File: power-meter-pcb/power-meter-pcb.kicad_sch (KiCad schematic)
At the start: 12 parts, among them J1 USB4105-GF-A, J2 Debug, SW1 EN, SW2 BOOT, U1 TPD3E001DRLR, U2 ESP32-S3-WROOM-1

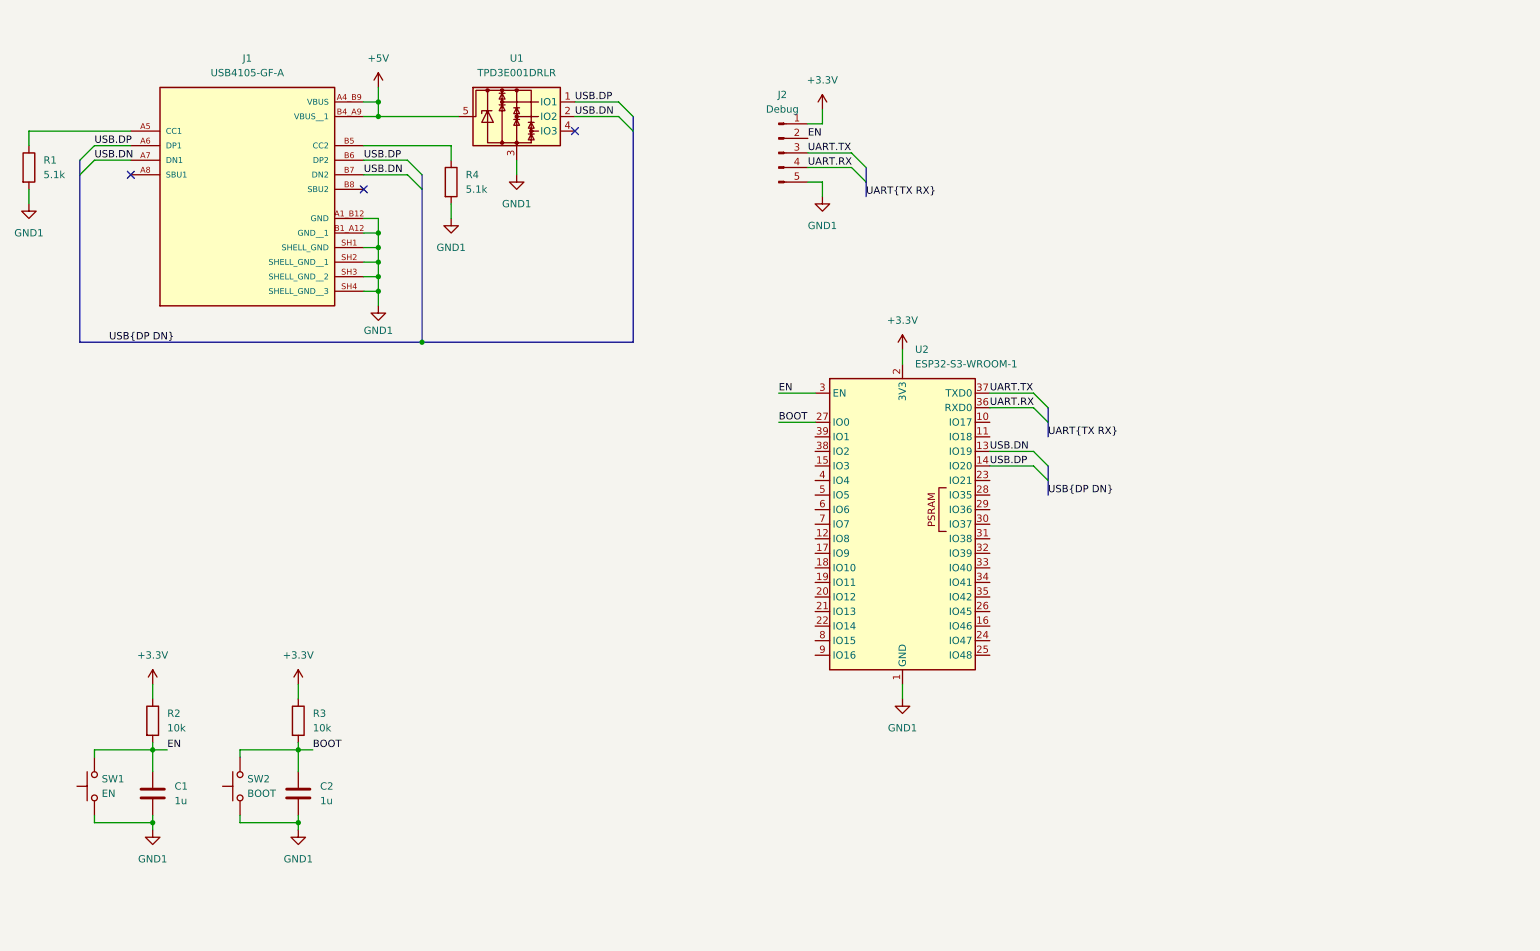
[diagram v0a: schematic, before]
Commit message: Added amplifier, IMU, inter board connections
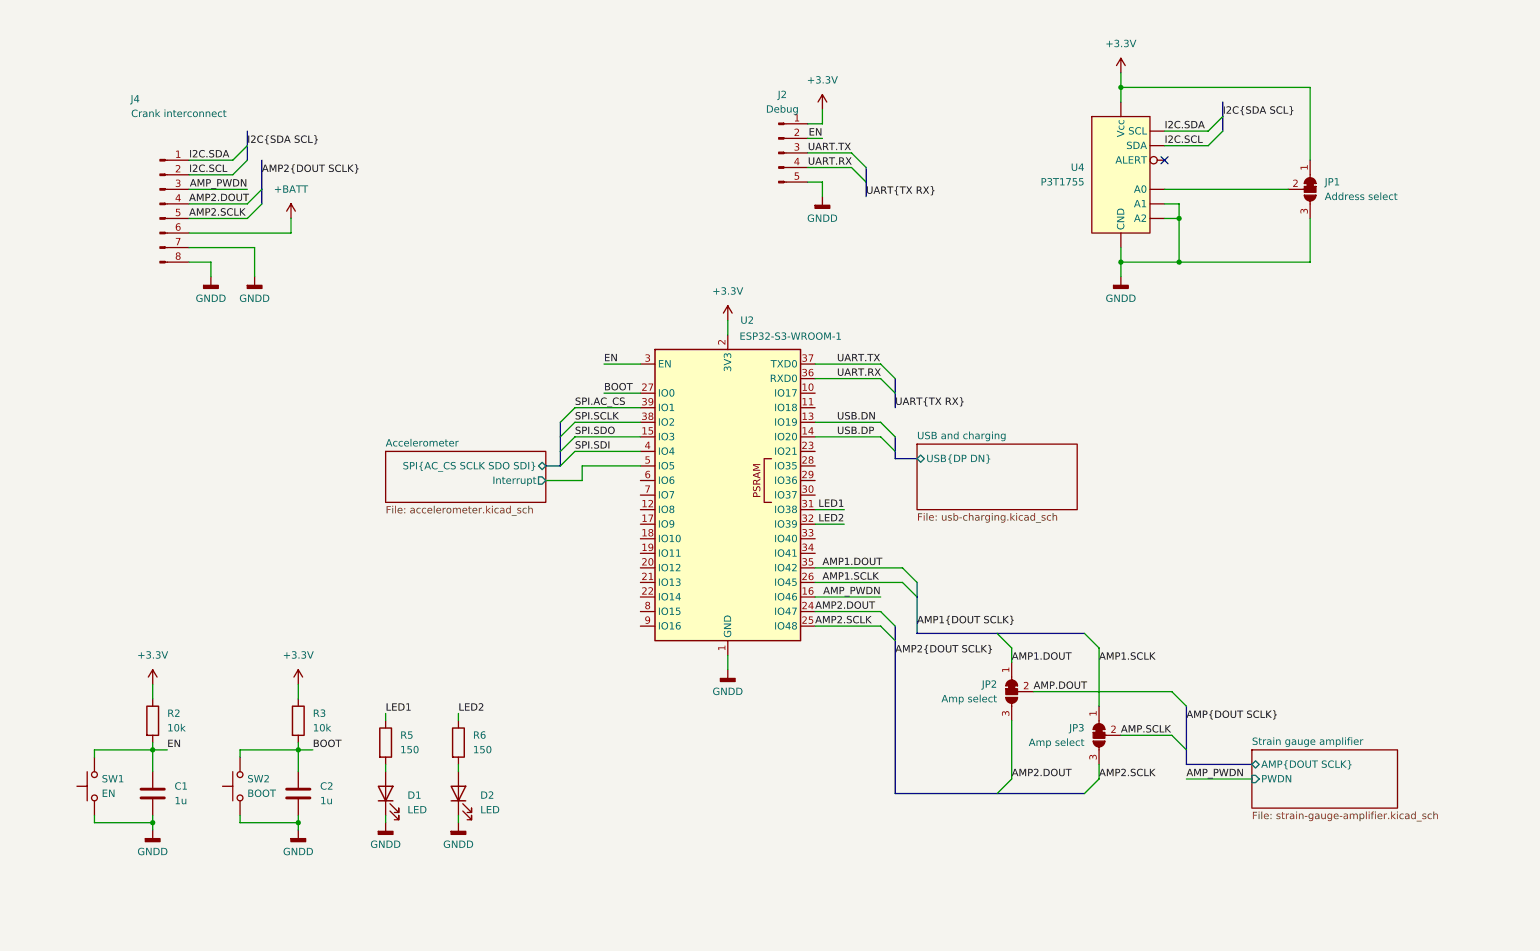
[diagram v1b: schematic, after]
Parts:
- removed J1: USB4105-GF-A, USB4105-GF-A:GCT_USB4105-GF-A, symbol USB4105:USB4105-GF-A
- removed R1, R4: 5.1k, symbol Device:R
- removed U1: TPD3E001DRLR, Package_TO_SOT_SMD:SOT-553, symbol Power_Protection:TPD3E001DRLR
- added D1, D2: LED, symbol Device:LED
- added J4: Crank interconnect, symbol Connector:Conn_01x08_Pin
- added JP1: Address select, symbol Jumper:SolderJumper_3_Bridged12
- added JP2, JP3: Amp select, symbol Jumper:SolderJumper_3_Bridged12
- added R5, R6: 150, symbol Device:R
- added U4: P3T1755, Package_SO:TSSOP-8_3x3mm_P0.65mm, symbol Custom:P3T1755_Temperature_sensor
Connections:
- net +3.3V: now also JP1.1 (A), U4. (Vcc)
- net SPI.SDO: now reaches U2.15 (IO3)
- net AMP_PWDN: now reaches U2.16 (IO46)
- net AMP_PWDN: now also J4.3 (Pin_3)
- net AMP2.DOUT: now reaches U2.24 (IO47)
- net AMP2.DOUT: now also J4.4 (Pin_4), JP2.3 (B)
- net AMP2.SCLK: now reaches U2.25 (IO48)
- net AMP2.SCLK: now also J4.5 (Pin_5), JP3.3 (B)
- net AMP1.SCLK: now reaches U2.26 (IO45)
- net AMP1.SCLK: now also JP3.1 (A)
- net LED1: now reaches U2.31 (IO38)
- net LED1: now also R5.1
- net LED2: now reaches U2.32 (IO39)
- net LED2: now also R6.1
- net AMP1.DOUT: now reaches U2.35 (IO42)
- net AMP1.DOUT: now also JP2.1 (A)
- net SPI.SCLK: now reaches U2.38 (IO2)
- net SPI.AC_CS: now reaches U2.39 (IO1)
- net SPI.SDI: now reaches U2.4 (IO4)
- net Accelerometer/Interrupt: now reaches U2.5 (IO5)
- net GND1 renamed GNDD
- net GNDD: now also D1.1 (K), D2.1 (K), J4.7 (Pin_7), J4.8 (Pin_8), JP1.3 (B), U4. (Vcc)
- new net: JP1.2 (C), U4. (Vcc)
- new net: D2.2 (A), R6.2
- new net: D1.2 (A), R5.2
- new net +BATT: J4.6 (Pin_6)
- new net AMP.DOUT: JP2.2 (C)
- new net AMP.SCLK: JP3.2 (C)
- new net I2C.SCL: J4.2 (Pin_2), U4. (Vcc)
- new net I2C.SDA: J4.1 (Pin_1), U4. (Vcc)
- no-connect marks 3 -> 1
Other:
- added sheet Accelerometer (accelerometer.kicad_sch)
- added sheet Strain gauge amplifier (strain-gauge-amplifier.kicad_sch)
- added sheet USB and charging (usb-charging.kicad_sch)
- moved on the sheet: U2

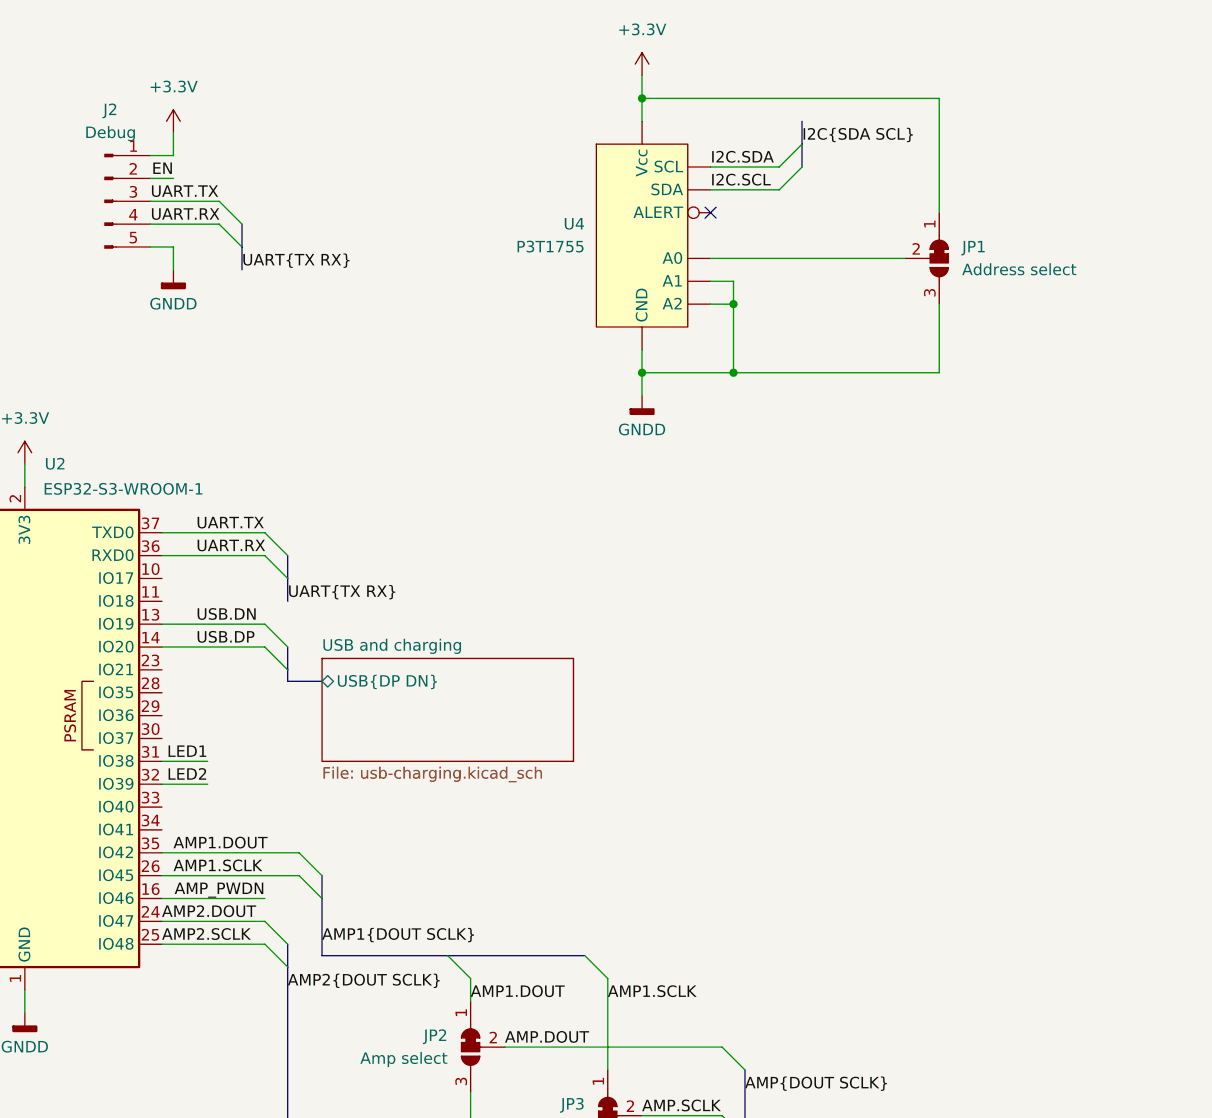
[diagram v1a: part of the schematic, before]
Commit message: Assigning footprints, extremely rough idea of size
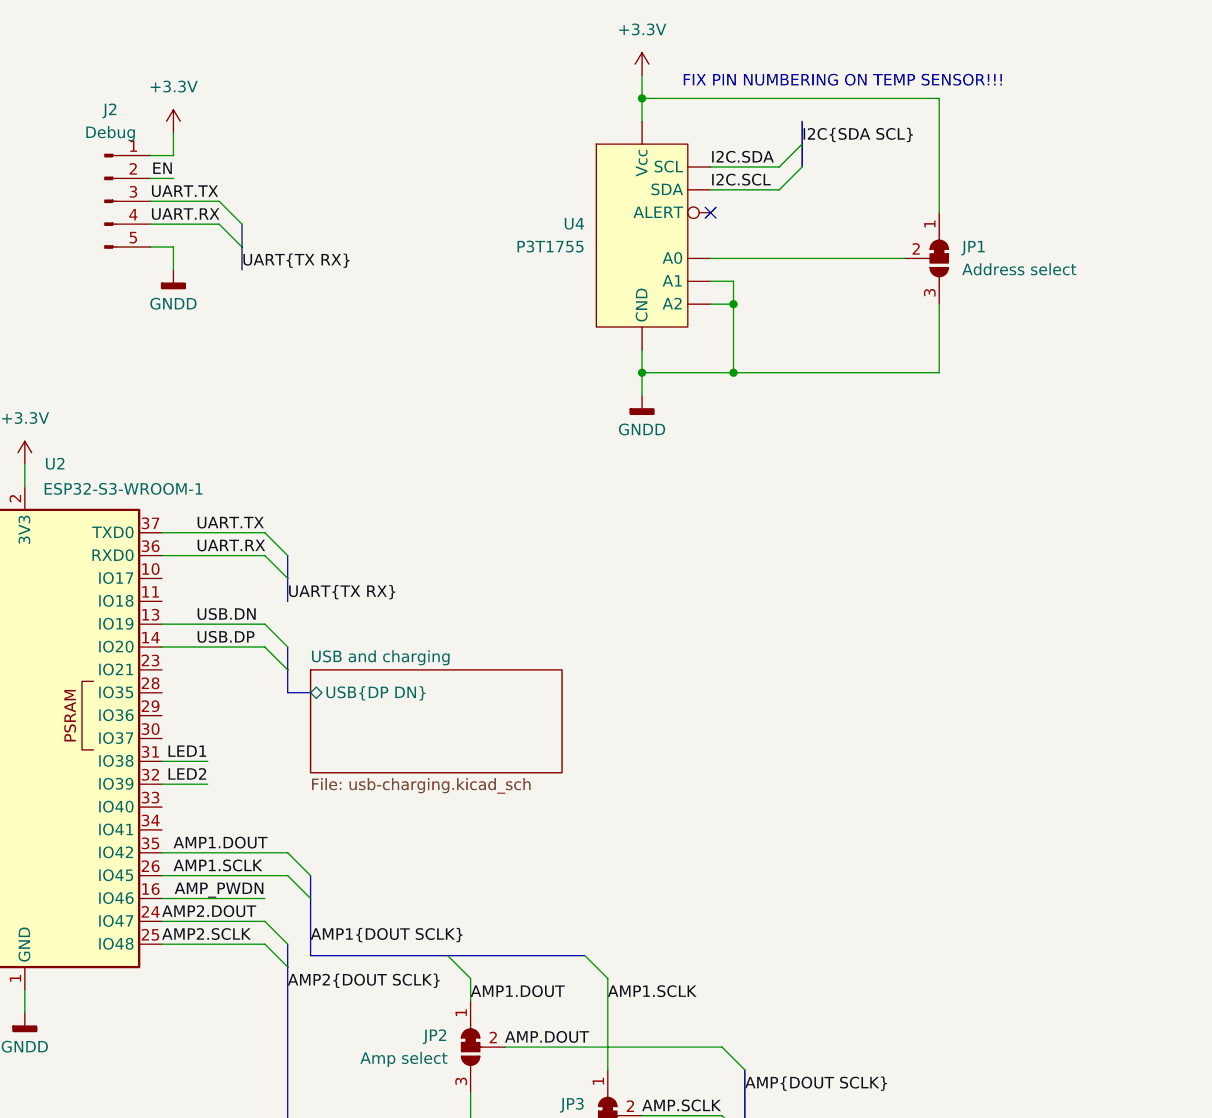
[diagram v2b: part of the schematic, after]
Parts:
- C1, C2: footprint (none) -> Capacitor_SMD:C_0603_1608Metric_Pad1.08x0.95mm_HandSolder
- D1, D2: footprint (none) -> LED_SMD:LED_0603_1608Metric_Pad1.05x0.95mm_HandSolder
- J2: footprint (none) -> Connector_PinHeader_2.54mm:PinHeader_1x05_P2.54mm_Vertical
- J4: footprint (none) -> Connector_PinHeader_2.54mm:PinHeader_1x08_P2.54mm_Vertical
- JP1, JP2, JP3: footprint (none) -> Jumper:SolderJumper-3_P1.3mm_Open_RoundedPad1.0x1.5mm
- R2, R3, R5, R6: footprint (none) -> Resistor_SMD:R_0603_1608Metric_Pad0.98x0.95mm_HandSolder
- SW1, SW2: footprint (none) -> Button_Switch_SMD:SW_Push_1P1T_NO_CK_KMR2
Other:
- note added: "FIX PIN NUMBERING ON TEMP SENSOR!!!"
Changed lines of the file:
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@@
 	)
 	(bus_entry
-		(at 176.53 121.92)
+		(at 175.26 121.92)
 		(size 2.54 2.54)
 		(stroke
@@
 	)
 	(bus_entry
-		(at 176.53 124.46)
+		(at 175.26 124.46)
 		(size 2.54 2.54)
 		(stroke
@@
 	(bus
 		(pts
-			(xy 179.07 102.87) (xy 175.26 102.87)
+			(xy 177.8 104.14) (xy 175.26 104.14)
 		)
 		(stroke
@@
 	(bus
 		(pts
-			(xy 179.07 127) (xy 179.07 133.35)
+			(xy 177.8 127) (xy 177.8 133.35)
 		)
 		(stroke
@@
 	(bus
 		(pts
-			(xy 175.26 101.6) (xy 175.26 102.87)
+			(xy 175.26 101.6) (xy 175.26 104.14)
 		)
 		(stroke
@@
 	(wire
 		(pts
-			(xy 161.29 121.92) (xy 176.53 121.92)
+			(xy 161.29 121.92) (xy 175.26 121.92)
 		)
 		(stroke
@@
 	(bus
 		(pts
-			(xy 179.07 133.35) (xy 193.04 133.35)
+			(xy 177.8 133.35) (xy 193.04 133.35)
 		)
 		(stroke
@@
 	(wire
 		(pts
-			(xy 161.29 124.46) (xy 176.53 124.46)
+			(xy 161.29 124.46) (xy 175.26 124.46)
 		)
 		(stroke
@@
 	(bus
 		(pts
-			(xy 179.07 124.46) (xy 179.07 127)
+			(xy 177.8 124.46) (xy 177.8 127)
 		)
 		(stroke
@@
 		)
 	)
+	(text "FIX PIN NUMBERING ON TEMP SENSOR!!!"
+		(exclude_from_sim no)
+		(at 236.982 36.322 0)
+		(effects
+			(font
+				(size 1.27 1.27)
+			)
+		)
+	)
 	(label "BOOT"
 		(at 73.66 153.67 0)
@@
 	)
 	(label "AMP1{DOUT SCLK}"
-		(at 179.07 132.08 0)
+		(at 177.8 132.08 0)
 		(fields_autoplaced yes)
 		(effects
@@
 			)
 		)
-		(property "Footprint" ""
+		(property "Footprint" "Button_Switch_SMD:SW_Push_1P1T_NO_CK_KMR2"
 			(at 30.48 160.02 0)
 			(effects
@@
 			)
 		)
-		(property "Footprint" ""
+		(property "Footprint" "Jumper:SolderJumper-3_P1.3mm_Open_RoundedPad1.0x1.5mm"
 			(at 195.58 143.51 0)
 			(effects
@@
 			)
 		)
-		(property "Footprint" ""
+		(property "Footprint" "Capacitor_SMD:C_0603_1608Metric_Pad1.08x0.95mm_HandSolder"
 			(at 44.7548 157.48 0)
 			(effects
@@
 			)
 		)
-		(property "Footprint" ""
+		(property "Footprint" "Connector_PinHeader_2.54mm:PinHeader_1x08_P2.54mm_Vertical"
 			(at 46.99 58.42 0)
 			(effects
@@
 			)
 		)
-		(property "Footprint" ""
+		(property "Footprint" "Resistor_SMD:R_0603_1608Metric_Pad0.98x0.95mm_HandSolder"
 			(at 43.942 148.59 90)
 			(effects
@@
 			)
 		)
-		(property "Footprint" ""
+		(property "Footprint" "Resistor_SMD:R_0603_1608Metric_Pad0.98x0.95mm_HandSolder"
 			(at 69.342 148.59 90)
 			(effects
@@
 			)
 		)
-		(property "Footprint" ""
+		(property "Footprint" "Resistor_SMD:R_0603_1608Metric_Pad0.98x0.95mm_HandSolder"
 			(at 97.282 152.4 90)
 			(effects
@@
 			)
 		)
-		(property "Footprint" ""
+		(property "Footprint" "Connector_PinHeader_2.54mm:PinHeader_1x05_P2.54mm_Vertical"
 			(at 154.94 49.53 0)
 			(effects
@@
 			)
 		)
-		(property "Footprint" ""
+		(property "Footprint" "Button_Switch_SMD:SW_Push_1P1T_NO_CK_KMR2"
 			(at 55.88 160.02 0)
 			(effects
@@
 			)
 		)
-		(property "Footprint" ""
+		(property "Footprint" "Jumper:SolderJumper-3_P1.3mm_Open_RoundedPad1.0x1.5mm"
 			(at 247.65 55.88 0)
 			(effects
@@
 			)
 		)
-		(property "Footprint" ""
+		(property "Footprint" "LED_SMD:LED_0603_1608Metric_Pad1.05x0.95mm_HandSolder"
 			(at 86.36 161.29 0)
 			(effects
@@
 			)
 		)
-		(property "Footprint" ""
+		(property "Footprint" "LED_SMD:LED_0603_1608Metric_Pad1.05x0.95mm_HandSolder"
 			(at 99.06 161.29 0)
 			(effects
@@
 			)
 		)
-		(property "Footprint" ""
+		(property "Footprint" "Resistor_SMD:R_0603_1608Metric_Pad0.98x0.95mm_HandSolder"
 			(at 84.582 152.4 90)
 			(effects
@@
 			)
 		)
-		(property "Footprint" ""
+		(property "Footprint" "Jumper:SolderJumper-3_P1.3mm_Open_RoundedPad1.0x1.5mm"
 			(at 210.82 151.13 0)
 			(effects
@@
 			)
 		)
-		(property "Footprint" ""
+		(property "Footprint" "Capacitor_SMD:C_0603_1608Metric_Pad1.08x0.95mm_HandSolder"
 			(at 70.1548 157.48 0)
 			(effects
@@
 	)
 	(sheet
-		(at 179.07 100.33)
+		(at 177.8 101.6)
 		(size 27.94 11.43)
 		(fields_autoplaced yes)
@@
 		)
 		(property "Sheetname" "USB and charging"
-			(at 179.07 99.6184 0)
+			(at 177.8 100.8884 0)
 			(effects
 				(font
@@
 		)
 		(property "Sheetfile" "usb-charging.kicad_sch"
-			(at 179.07 112.3446 0)
+			(at 177.8 113.6146 0)
 			(effects
 				(font
@@
 		)
 		(pin "USB{DP DN}" bidirectional
-			(at 179.07 102.87 180)
+			(at 177.8 104.14 180)
 			(effects
 				(font

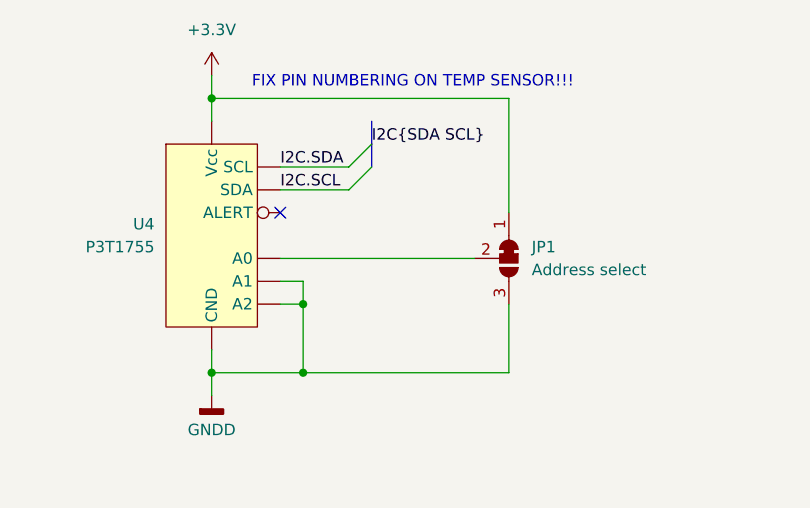
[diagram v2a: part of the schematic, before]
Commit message: Added power supply to PCB
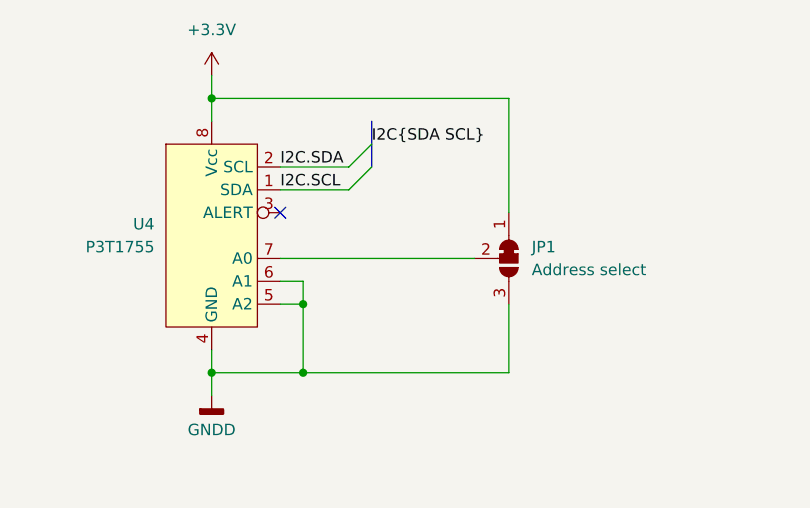
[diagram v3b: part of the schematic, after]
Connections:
- net +3.3V: now also U4.8 (Vcc); no longer U4. (Vcc)
- net GNDD: now also U4.4 (GND), U4.5 (A2), U4.6 (A1); no longer U4. (Vcc)
- net I2C.SCL: now also U4.1 (SDA); no longer U4. (Vcc)
- net I2C.SDA: now also U4.2 (SCL); no longer U4. (Vcc)
- net at JP1.2 (C): now also U4.7 (A0); no longer U4. (Vcc)
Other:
- note removed: "FIX PIN NUMBERING ON TEMP SENSOR!!!"
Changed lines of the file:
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@@
-		)
-	)
-	(text "FIX PIN NUMBERING ON TEMP SENSOR!!!"
-		(exclude_from_sim no)
-		(at 236.982 36.322 0)
-		(effects
-			(font
-				(size 1.27 1.27)
-			)
 		)
 	)
@@
 			)
 		)
-		(pin ""
-		)
-		(pin ""
-		)
-		(pin ""
-		)
-		(pin ""
-		)
-		(pin ""
-		)
-		(pin ""
-		)
-		(pin ""
-		)
-		(pin ""
+		(pin "8"
+		)
+		(pin "2"
+		)
+		(pin "6"
+		)
+		(pin "4"
+		)
+		(pin "3"
+		)
+		(pin "1"
+		)
+		(pin "5"
+		)
+		(pin "7"
 		)
 		(instances

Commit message: Started PCB layout
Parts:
- renumbered J4 to J1, JP2 to JP1, JP3 to JP2, JP1 to JP3, R2 to R1, R3 to R2, R5 to R3, R6 to R4, U2 to U1, U4 to U2
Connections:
- net USB and charging/Battery voltage: now reaches U1.11 (IO18)
- net USB and charging/Power save: now reaches U1.23 (IO21)
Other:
- sheet USB and charging ports: added Battery voltage, Power save; removed none
- moved on the sheet: C1, C2, D1, D2, R1, R2, R3, R4, SW1, SW2
